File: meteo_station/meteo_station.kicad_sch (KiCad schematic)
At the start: 20 parts, among them SW1 SW_SPDT, U1 TP4056, U2 LF33_TO220, U3 ESP32-WROOM, U4 DS18B20, U5 BH1750, U6 BME280

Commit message: PCB v2
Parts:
- D1, D2: footprint Diode_SMD:D_SMB_Handsoldering -> Diode_SMD:D_SMB
- U2: footprint Package_TO_SOT_THT:TO-220-3_Vertical -> Package_TO_SOT_THT:TO-220-3_Horizontal_TabDown
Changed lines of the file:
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@@
     (property "Reference" "D2" (id 0) (at 40.64 67.31 0))
     (property "Value" "D_Schottky" (id 1) (at 40.64 74.93 0))
-    (property "Footprint" "Diode_SMD:D_SMB_Handsoldering" (id 2) (at 40.64 71.12 0)
+    (property "Footprint" "Diode_SMD:D_SMB" (id 2) (at 40.64 71.12 0)
       (effects (font (size 1.27 1.27)) hide)
     )
@@
     (property "Reference" "U2" (id 0) (at 123.19 17.78 0))
     (property "Value" "LF33_TO220" (id 1) (at 123.19 20.32 0))
-    (property "Footprint" "Package_TO_SOT_THT:TO-220-3_Vertical" (id 2) (at 123.19 18.415 0)
+    (property "Footprint" "Package_TO_SOT_THT:TO-220-3_Horizontal_TabDown" (id 2) (at 123.19 18.415 0)
       (effects (font (size 1.27 1.27) italic) hide)
     )
@@
     (property "Reference" "D1" (id 0) (at 40.64 52.07 0))
     (property "Value" "D_Schottky" (id 1) (at 40.64 59.69 0))
-    (property "Footprint" "Diode_SMD:D_SMB_Handsoldering" (id 2) (at 40.64 55.88 0)
+    (property "Footprint" "Diode_SMD:D_SMB" (id 2) (at 40.64 55.88 0)
       (effects (font (size 1.27 1.27)) hide)
     )
@@
     )
     (path "/e7b413b3-1f93-48aa-a026-394b6c5972c0"
-      (reference "D1") (unit 1) (value "D_Schottky") (footprint "Diode_SMD:D_SMB_Handsoldering")
+      (reference "D1") (unit 1) (value "D_Schottky") (footprint "Diode_SMD:D_SMB")
     )
     (path "/685a39c3-6e72-4542-9e1d-6357409d8729"
-      (reference "D2") (unit 1) (value "D_Schottky") (footprint "Diode_SMD:D_SMB_Handsoldering")
+      (reference "D2") (unit 1) (value "D_Schottky") (footprint "Diode_SMD:D_SMB")
     )
     (path "/ea78ddbc-2970-428e-b50b-675425fbb699"
@@
     )
     (path "/cd3aea37-37f7-4673-bd53-2b06ffe90909"
-      (reference "U2") (unit 1) (value "LF33_TO220") (footprint "Package_TO_SOT_THT:TO-220-3_Vertical")
+      (reference "U2") (unit 1) (value "LF33_TO220") (footprint "Package_TO_SOT_THT:TO-220-3_Horizontal_TabDown")
     )
     (path "/93a49863-00ee-408b-9e67-37bd2abd68da"

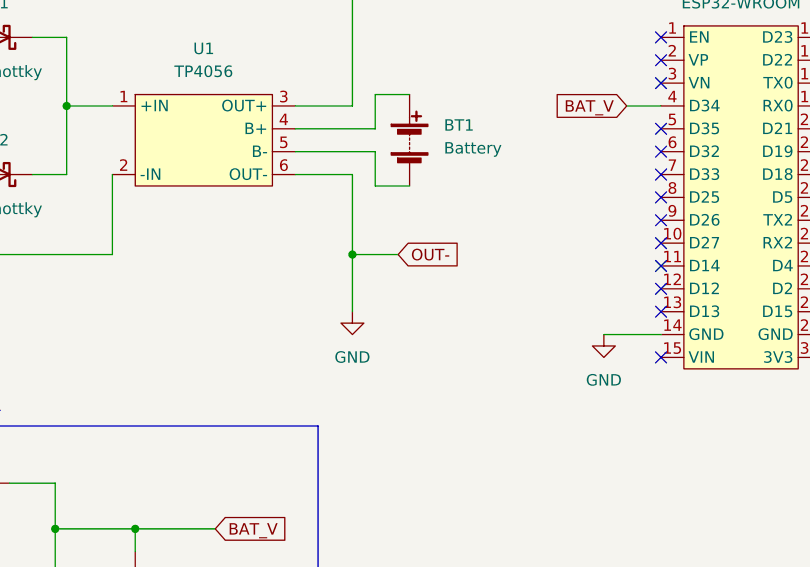
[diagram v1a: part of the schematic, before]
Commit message: Start working on logo
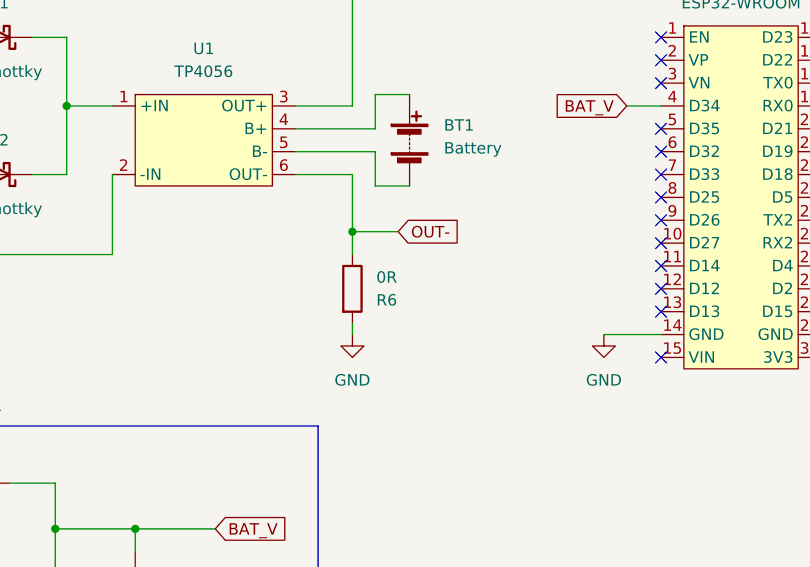
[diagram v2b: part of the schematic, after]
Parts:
- added R6: 0R, Resistor_SMD:R_0603_1608Metric, symbol Device:R
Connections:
- net GND: now also R6.2; no longer R2.2, U1.6 (OUT-)
- new net OUT-: R2.2, R6.1, U1.6 (OUT-)
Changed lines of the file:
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@@
   (junction (at 48.26 63.5) (diameter 0) (color 0 0 0 0)
   )
+  (junction (at 80.01 77.47) (diameter 0) (color 0 0 0 0)
+  )
   (junction (at 107.95 24.13) (diameter 0) (color 0 0 0 0)
   )
@@
   )
   (junction (at 166.37 76.2) (diameter 0) (color 0 0 0 0)
-  )
-  (junction (at 80.01 80.01) (diameter 0) (color 0 0 0 0)
   )
   (no_connect (at 93.98 29.21))
@@
     (stroke (width 0) (type default) (color 0 0 0 0))
   )
-  (wire (pts (xy 80.01 71.12) (xy 80.01 80.01))
+  (wire (pts (xy 80.01 71.12) (xy 80.01 77.47))
     (stroke (width 0) (type default) (color 0 0 0 0))
   )
@@
     (stroke (width 0) (type default) (color 0 0 0 0))
   )
-  (wire (pts (xy 80.01 80.01) (xy 85.09 80.01))
+  (wire (pts (xy 80.01 77.47) (xy 85.09 77.47))
     (stroke (width 0) (type default) (color 0 0 0 0))
   )
@@
     (stroke (width 0) (type default) (color 0 0 0 0))
   )
+  (wire (pts (xy 80.01 77.47) (xy 80.01 80.01))
+    (stroke (width 0) (type default) (color 0 0 0 0))
+  )
   (wire (pts (xy 73.66 68.58) (xy 82.55 68.58))
     (stroke (width 0) (type default) (color 0 0 0 0))
@@
     (stroke (width 0) (type default) (color 0 0 0 0))
   )
-  (wire (pts (xy 80.01 80.01) (xy 80.01 86.36))
-    (stroke (width 0) (type default) (color 0 0 0 0))
-  )
   (wire (pts (xy 166.37 76.2) (xy 168.91 76.2))
     (stroke (width 0) (type default) (color 0 0 0 0))
@@
   )
   (wire (pts (xy 130.81 24.13) (xy 135.89 24.13))
+    (stroke (width 0) (type default) (color 0 0 0 0))
+  )
+  (wire (pts (xy 80.01 87.63) (xy 80.01 88.9))
     (stroke (width 0) (type default) (color 0 0 0 0))
   )
@@
     )
   )
-  (global_label "OUT-" (shape input) (at 85.09 80.01 0) (fields_autoplaced)
+  (global_label "OUT-" (shape input) (at 85.09 77.47 0) (fields_autoplaced)
     (effects (font (size 1.27 1.27)) (justify left))
-    (property "Intersheet References" "${INTERSHEET_REFS}" (id 0) (at 92.7041 79.9306 0)
+    (property "Intersheet References" "${INTERSHEET_REFS}" (id 0) (at 92.7041 77.3906 0)
       (effects (font (size 1.27 1.27)) (justify left) hide)
     )
@@
     (pin "1")
   )
-  (symbol (lib_id "power:GND") (at 80.01 86.36 0) (unit 1)
-    (in_bom yes) (on_board yes) (fields_autoplaced)
-    (property "Reference" "#PWR02" (id 0) (at 80.01 92.71 0)
-      (effects (font (size 1.27 1.27)) hide)
-    )
-    (property "Value" "GND" (id 1) (at 80.01 91.44 0))
-    (property "Footprint" "" (id 2) (at 80.01 86.36 0)
-      (effects (font (size 1.27 1.27)) hide)
-    )
-    (property "Datasheet" "" (id 3) (at 80.01 86.36 0)
+  (symbol (lib_id "power:GND") (at 80.01 88.9 0) (unit 1)
+    (in_bom yes) (on_board yes) (fields_autoplaced)
+    (property "Reference" "#PWR02" (id 0) (at 80.01 95.25 0)
+      (effects (font (size 1.27 1.27)) hide)
+    )
+    (property "Value" "GND" (id 1) (at 80.01 93.98 0))
+    (property "Footprint" "" (id 2) (at 80.01 88.9 0)
+      (effects (font (size 1.27 1.27)) hide)
+    )
+    (property "Datasheet" "" (id 3) (at 80.01 88.9 0)
       (effects (font (size 1.27 1.27)) hide)
     )
@@
     )
     (pin "1")
+  )
+  (symbol (lib_id "Device:R") (at 80.01 83.82 0) (unit 1)
+    (in_bom yes) (on_board yes)
+    (property "Reference" "R6" (id 0) (at 83.82 85.09 0))
+    (property "Value" "0R" (id 1) (at 83.82 82.55 0))
+    (property "Footprint" "Resistor_SMD:R_0603_1608Metric" (id 2) (at 78.232 83.82 90)
+      (effects (font (size 1.27 1.27)) hide)
+    )
+    (property "Datasheet" "~" (id 3) (at 80.01 83.82 0)
+      (effects (font (size 1.27 1.27)) hide)
+    )
+    (pin "1")
+    (pin "2")
   )
   (symbol (lib_id "meteo_station_symbols:LF33_TO220") (at 123.19 24.13 0) (unit 1)
@@
       (reference "R5") (unit 1) (value "4.7K") (footprint "Resistor_SMD:R_0603_1608Metric")
     )
+    (path "/caae6352-8ebc-4ea9-9252-f672aba2fffc"
+      (reference "R6") (unit 1) (value "0R") (footprint "Resistor_SMD:R_0603_1608Metric")
+    )
     (path "/3a74dea1-1510-40f9-ac26-652aca9a28c3"

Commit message: Add jumper & version
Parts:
- removed R6: 0R, Resistor_SMD:R_0603_1608Metric, symbol Device:R
- added JP1: SolderJumper, Jumper:SolderJumper-2_P1.3mm_Bridged_Pad1.0x1.5mm, symbol Jumper:SolderJumper_2_Bridged
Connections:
- net GND: now also JP1.1 (A)
- net OUT-: now also JP1.2 (B)
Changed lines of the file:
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@@
     (pin "1")
-  )
-  (symbol (lib_id "Device:R") (at 80.01 83.82 0) (unit 1)
-    (in_bom yes) (on_board yes)
-    (property "Reference" "R6" (id 0) (at 83.82 85.09 0))
-    (property "Value" "0R" (id 1) (at 83.82 82.55 0))
-    (property "Footprint" "Resistor_SMD:R_0603_1608Metric" (id 2) (at 78.232 83.82 90)
-      (effects (font (size 1.27 1.27)) hide)
-    )
-    (property "Datasheet" "~" (id 3) (at 80.01 83.82 0)
-      (effects (font (size 1.27 1.27)) hide)
-    )
-    (pin "1")
-    (pin "2")
   )
   (symbol (lib_id "meteo_station_symbols:LF33_TO220") (at 123.19 24.13 0) (unit 1)
@@
     (pin "2")
   )
+  (symbol (lib_id "Jumper:SolderJumper_2_Bridged") (at 80.01 83.82 90) (unit 1)
+    (in_bom yes) (on_board yes) (fields_autoplaced)
+    (property "Reference" "JP1" (id 0) (at 82.55 82.5499 90)
+      (effects (font (size 1.27 1.27)) (justify right))
+    )
+    (property "Value" "SolderJumper" (id 1) (at 82.55 85.0899 90)
+      (effects (font (size 1.27 1.27)) (justify right))
+    )
+    (property "Footprint" "Jumper:SolderJumper-2_P1.3mm_Bridged_Pad1.0x1.5mm" (id 2) (at 80.01 83.82 0)
+      (effects (font (size 1.27 1.27)) hide)
+    )
+    (property "Datasheet" "~" (id 3) (at 80.01 83.82 0)
+      (effects (font (size 1.27 1.27)) hide)
+    )
+    (pin "1")
+    (pin "2")
+  )
   (symbol (lib_id "Device:R") (at 38.1 105.41 270) (unit 1)
     (in_bom yes) (on_board yes)
@@
       (reference "D2") (unit 1) (value "D_Schottky") (footprint "Diode_SMD:D_SMB")
     )
+    (path "/e9febdd1-669e-46f3-983e-2ded7b5fa339"
+      (reference "JP1") (unit 1) (value "SolderJumper") (footprint "Jumper:SolderJumper-2_P1.3mm_Bridged_Pad1.0x1.5mm")
+    )
     (path "/ea78ddbc-2970-428e-b50b-675425fbb699"
       (reference "R1") (unit 1) (value "10K") (footprint "Resistor_SMD:R_0603_1608Metric")
@@
       (reference "R5") (unit 1) (value "4.7K") (footprint "Resistor_SMD:R_0603_1608Metric")
     )
-    (path "/caae6352-8ebc-4ea9-9252-f672aba2fffc"
-      (reference "R6") (unit 1) (value "0R") (footprint "Resistor_SMD:R_0603_1608Metric")
-    )
     (path "/3a74dea1-1510-40f9-ac26-652aca9a28c3"

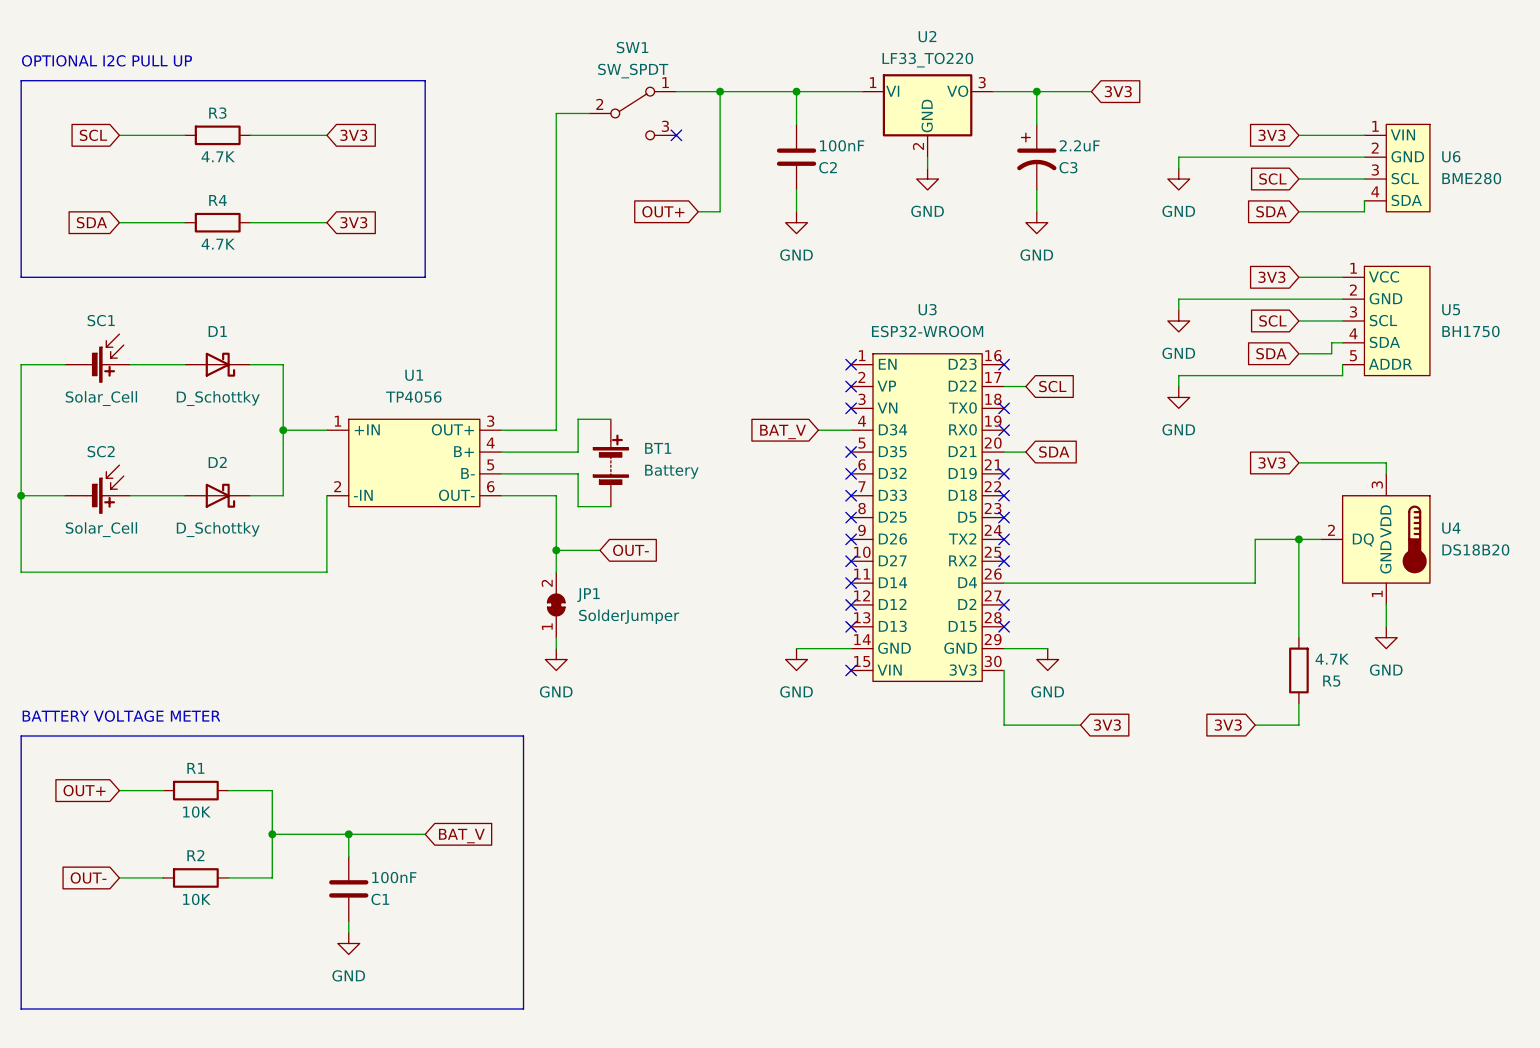
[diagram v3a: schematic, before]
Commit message: Add supercapacitor and 100nF
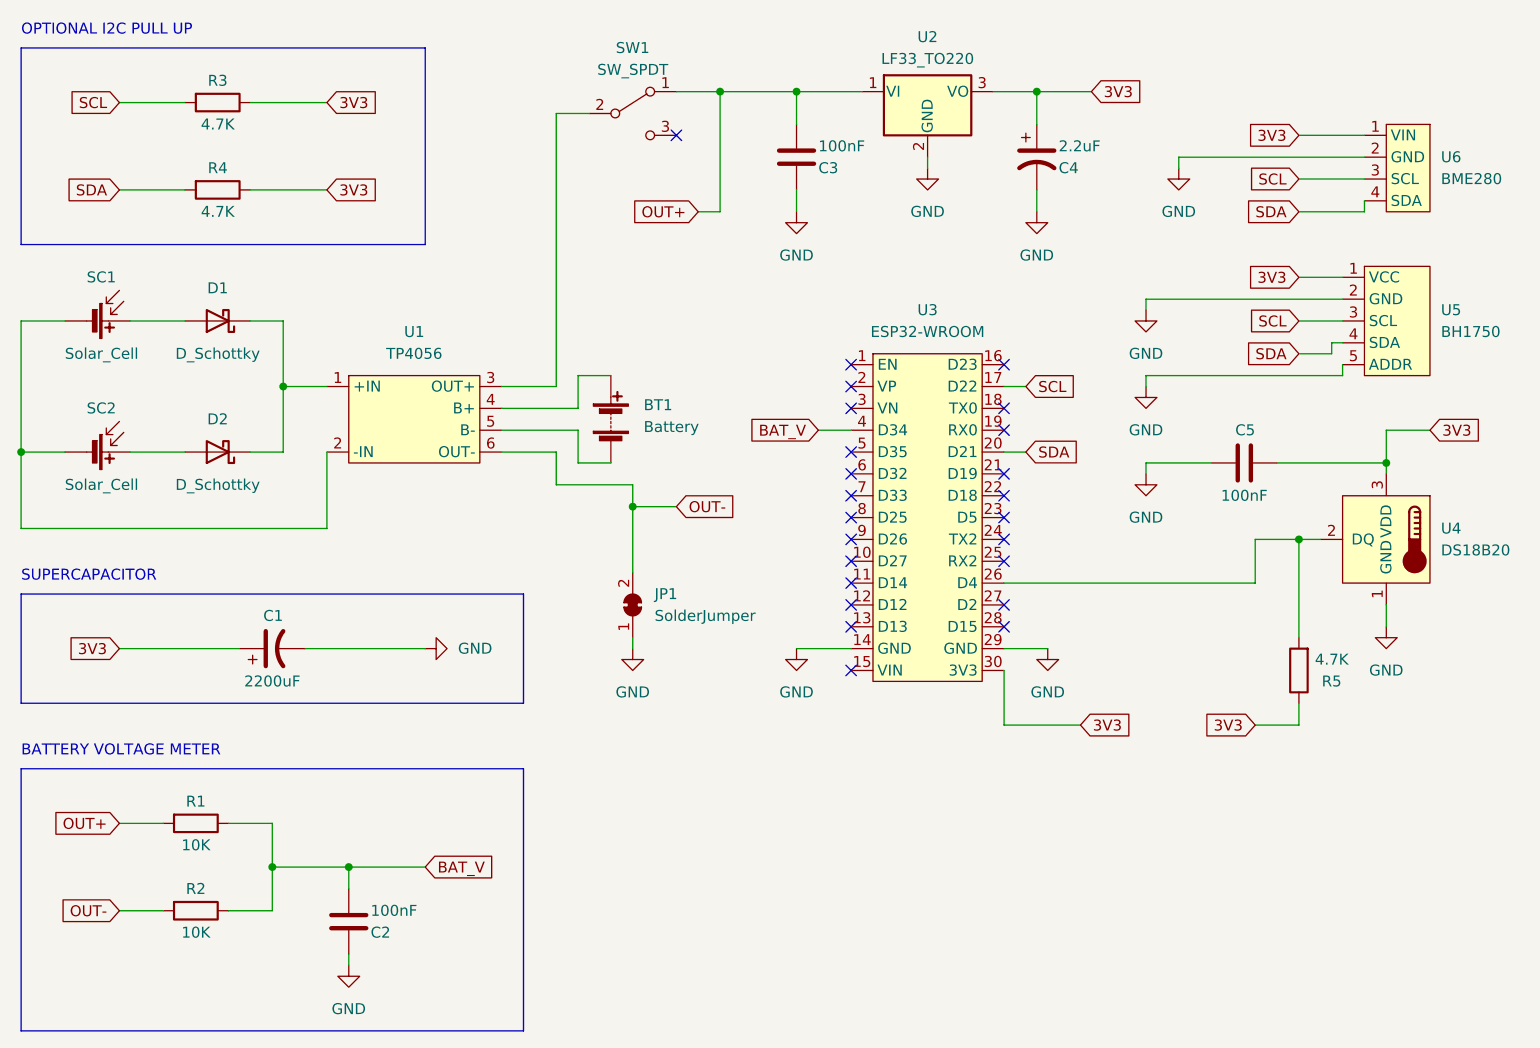
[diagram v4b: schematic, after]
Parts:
- added C1: 2200uF, Capacitor_THT:CP_Radial_D10.0mm_P5.00mm, symbol Device:C_Polarized_US
- added C5: 100nF, Capacitor_SMD:C_0603_1608Metric, symbol Device:C
- renumbered C1 to C2, C2 to C3, C3 to C4
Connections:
- net 3V3: now also C1.1, C5.2
- net GND: now also C1.2, C5.1
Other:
- note added: "SUPERCAPACITOR"
- moved on the sheet: BT1, C2, D1, D2, JP1, R1, R2, R3, R4, SC1, SC2, U1

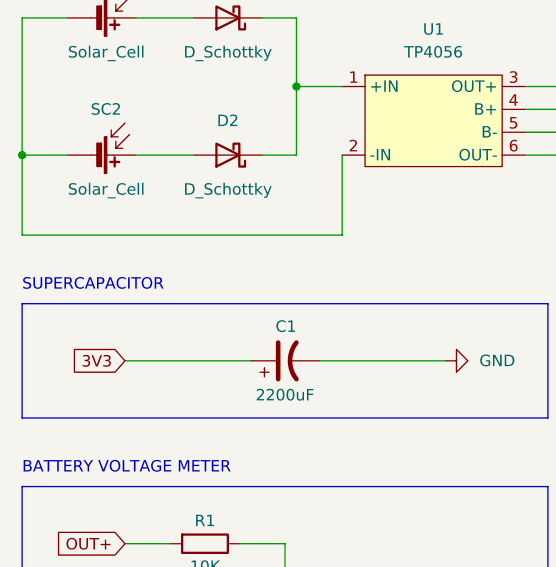
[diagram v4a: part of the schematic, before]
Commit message: Typo & label
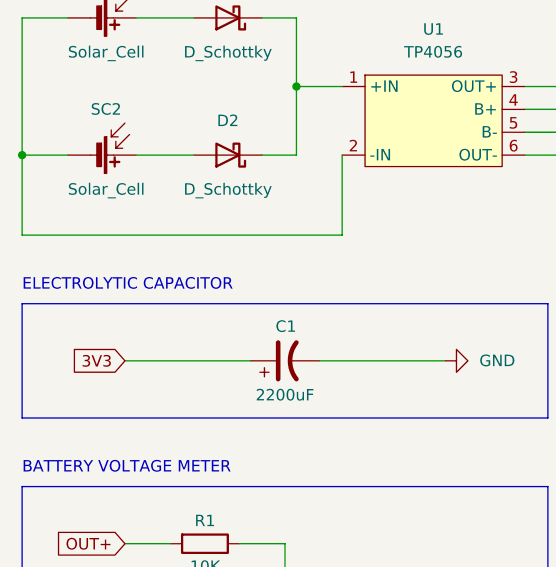
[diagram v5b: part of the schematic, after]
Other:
- note added: "ELECTROLYTIC CAPACITOR"
- note removed: "SUPERCAPACITOR"
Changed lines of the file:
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@@
     (effects (font (size 1.27 1.27)) (justify left bottom))
   )
-  (text "SUPERCAPACITOR" (at 17.78 81.28 0)
+  (text "ELECTROLYTIC CAPACITOR" (at 17.78 81.28 0)
     (effects (font (size 1.27 1.27)) (justify left bottom))
   )
